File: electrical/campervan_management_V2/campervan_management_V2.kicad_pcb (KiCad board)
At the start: 4 copper layers, 140 x 95 mm, 163 parts, among them J1 Battery & Fuse, J10 RS485, J11 Power On/Off Switch, J2 Battery 2, J3 Relays, J5 Input Flow Sensor, J6 Temp, J7 Output Flow Sensor, J8 Starter Battery, J9 Fans, K1 G6KU-2, Q1 Q_PMOS_DGS, Q10 Q_PMOS_DGS, Q2 Q_PMOS_DGS, Q4 MMBT2222A, Q6 MMBT2222A, Q7 Q_PMOS_DGS, Q8 Q_PMOS_DGS, Q9 Q_PMOS_DGS, SW1 SW_Push, U1 MCP16311T-E/MNS, U10 LM358DR2G, U11 LM358DR2G, U12 LTV-817S-TA1-C, U13 LTV-817S-TA1-C, U14 HCNR200-500E, U15 LM358DR2G, U16 LTV-817S-TA1-C, U17 LTV-817S-TA1-C, U18 LTV-817S-TA1-C, U19 MAX487E, U2 AMS1117-3.3, U20 LTV-817S-TA1-C, U21 LTV-817S-TA1-C, U22 LTV-817S-TA1-C, U23 LTV-817S-TA1-C, U24 LTV-817S-TA1-C, U25 MCP16311T-E/MNS, U3 LTV-817S-TA1-C, U4 HCNR200-500E, U5 AMS1117-3.3, U6 LM358DR2G, U7 LM358DR2G, U8 LTV-817S-TA1-C, U9 HCNR200-500E

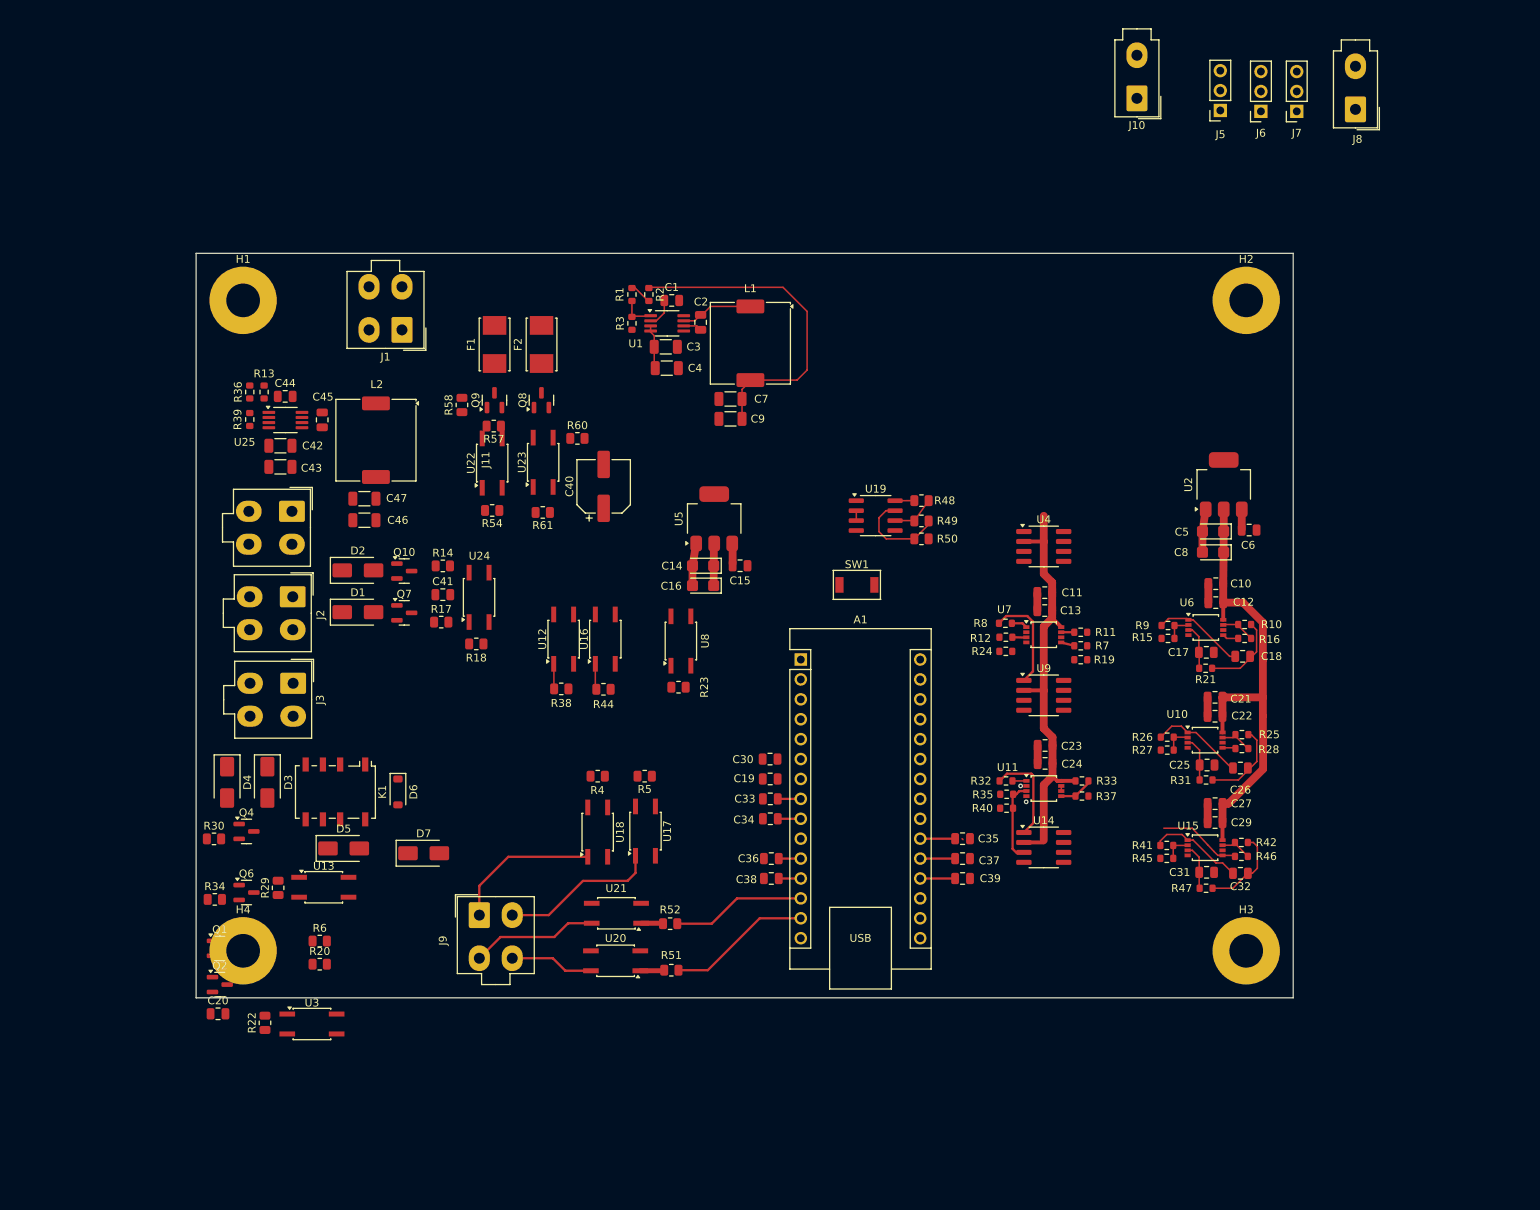
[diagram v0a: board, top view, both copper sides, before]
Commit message: First attempt at PCB layout
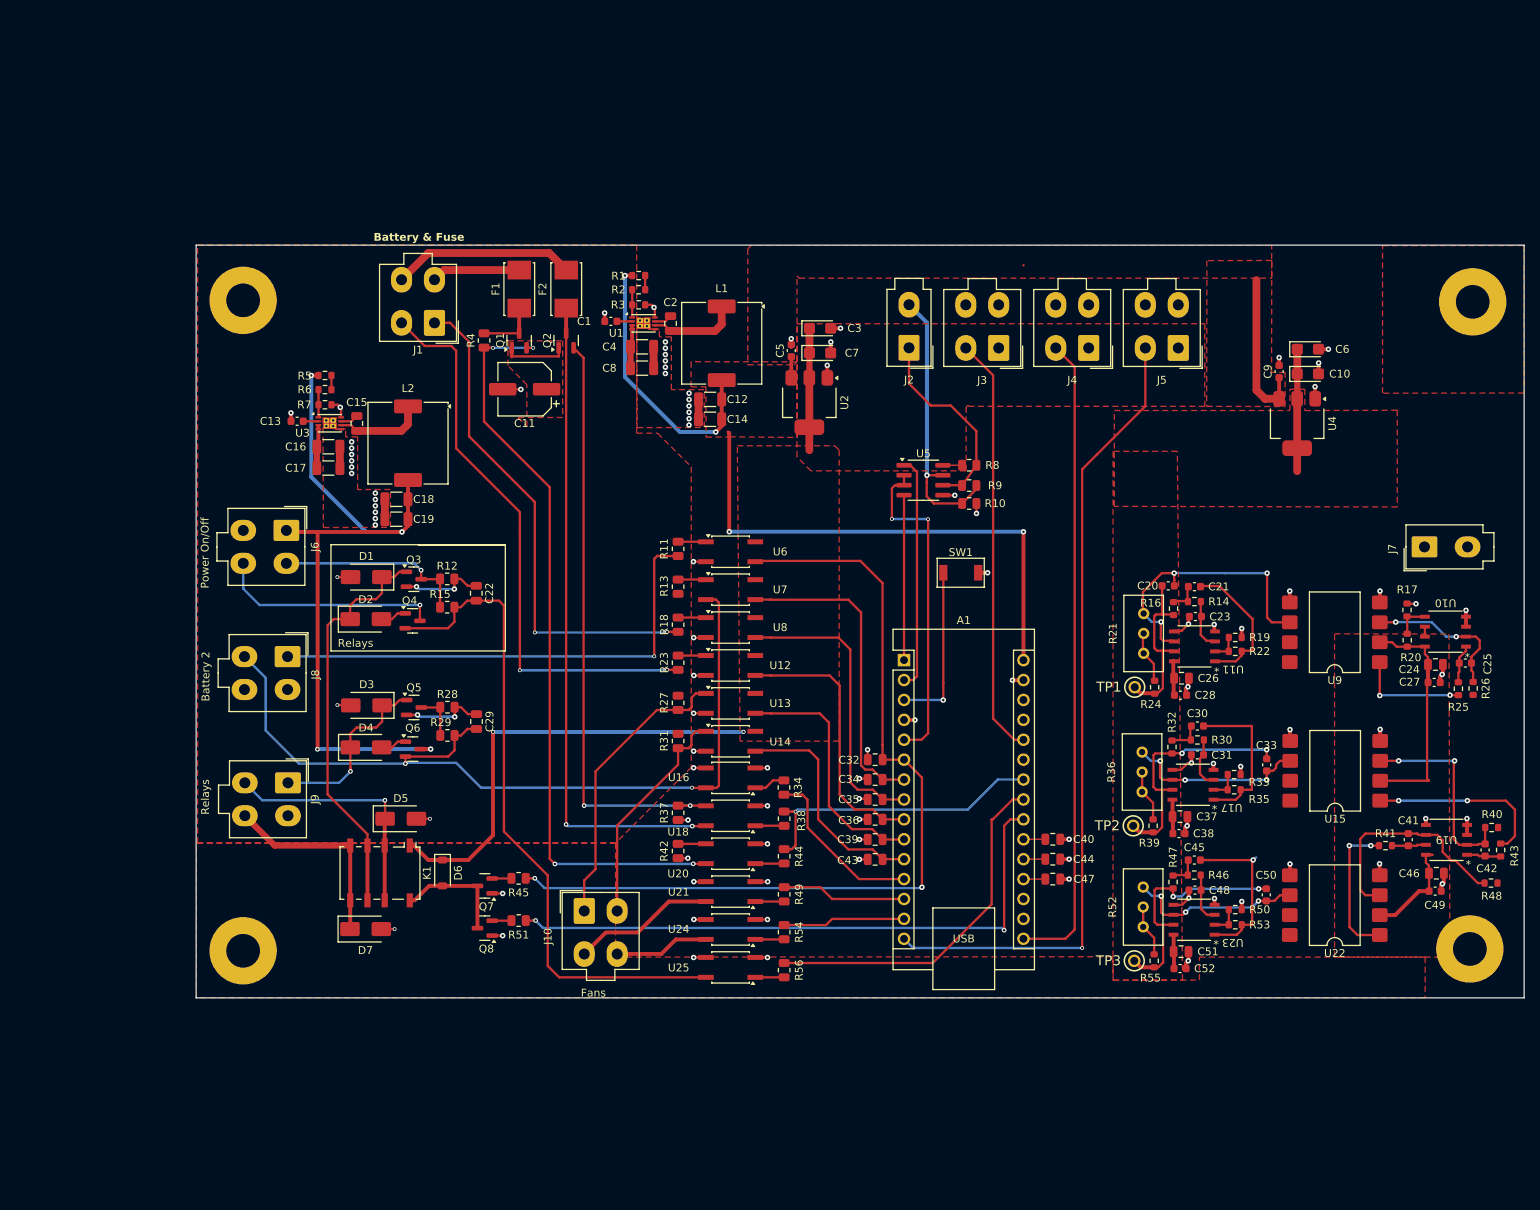
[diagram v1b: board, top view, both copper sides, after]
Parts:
- removed the C14 at (114.7, 94.9)
- removed the C15 at (119.4, 94.9)
- removed the C16 at (114.7, 97.4)
- removed the C8 at (179.8, 93.2)
- removed the J6 at (185.9, 36.9)
- removed the J7 at (190.4, 36.9)
- removed the R19 at (162.9, 106.9)
- removed the R24 at (153.3, 105.8)
- removed the R40 at (153.4, 125.8)
- removed the U5 at (116.1, 88.9)
- added C10: 10uF, Capacitor_Tantalum_SMD:CP_EIA-3216-18_Kemet-A, F.Cu at (191.9, 70.4)
- added C20: C_Small, Capacitor_SMD:C_0603_1608Metric, F.Cu at (174.0, 97.4)
- added C25: C_Small, Capacitor_SMD:C_0603_1608Metric, F.Cu at (212.0, 107.3)
- added C3: 10uF, Capacitor_Tantalum_SMD:CP_EIA-3216-18_Kemet-A, F.Cu at (129.6, 64.6)
- added C33: C_Small, Capacitor_SMD:C_0603_1608Metric, F.Cu at (186.6, 120.3)
- added C41: C_Small, Capacitor_SMD:C_0603_1608Metric, F.Cu at (204.7, 129.8)
- added C42: C_Small, Capacitor_SMD:C_0603_1608Metric, F.Cu at (214.5, 131.1)
- added C50: C_Small, Capacitor_SMD:C_0603_1608Metric, F.Cu at (186.6, 136.9)
- added C7: 10uF, Capacitor_Tantalum_SMD:CP_EIA-3216-18_Kemet-A, F.Cu at (129.6, 67.7)
- added C9: 1uF, Capacitor_SMD:C_0603_1608Metric, F.Cu at (188.2, 70.1)
- added J3: Temp, Connector_Molex:Molex_Mini-Fit_Jr_5566-04A_2x02_P4.20mm_Vertical, F.Cu at (152.4, 67.1)
- added J4: Output Flow Sensor, Connector_Molex:Molex_Mini-Fit_Jr_5566-04A_2x02_P4.20mm_Vertical, F.Cu at (163.9, 67.1)
- added R21: 10k, Potentiometer_THT:Potentiometer_Bourns_3296W_Vertical, F.Cu at (170.9, 106.0)
- added R36: 10k, Potentiometer_THT:Potentiometer_Bourns_3296W_Vertical, F.Cu at (170.7, 123.7)
- added R52: 10k, Potentiometer_THT:Potentiometer_Bourns_3296W_Vertical, F.Cu at (170.9, 141.0)
- added TP1: TestPoint, CV_connector:5000, F.Cu at (169.8, 110.4)
- added TP2: TestPoint, CV_connector:5000, F.Cu at (169.6, 128.1)
- added TP3: TestPoint, CV_connector:5000, F.Cu at (169.7, 145.3)
- added U4: AMS1117-3.3, Package_TO_SOT_SMD:SOT-223-3_TabPin2, F.Cu at (190.5, 76.7)
- C1: footprint Capacitor_SMD:C_0805_2012Metric -> Capacitor_SMD:C_0603_1608Metric
- C13: renamed from C44; footprint Capacitor_SMD:C_0805_2012Metric -> Capacitor_SMD:C_0603_1608Metric
- C21: renamed from C32; footprint Capacitor_SMD:C_0805_2012Metric -> Capacitor_SMD:C_0603_1608Metric
- C23: renamed from C31; footprint Capacitor_SMD:C_0805_2012Metric -> Capacitor_SMD:C_0603_1608Metric
- C27: renamed from C23; footprint Capacitor_SMD:C_0805_2012Metric -> Capacitor_SMD:C_0603_1608Metric
- C28: renamed from C27; footprint Capacitor_SMD:C_0805_2012Metric -> Capacitor_SMD:C_0603_1608Metric
- C30: renamed from C26; footprint Capacitor_SMD:C_0805_2012Metric -> Capacitor_SMD:C_0603_1608Metric
- C31: renamed from C25; footprint Capacitor_SMD:C_0805_2012Metric -> Capacitor_SMD:C_0603_1608Metric
- C38: renamed from C22; footprint Capacitor_SMD:C_0805_2012Metric -> Capacitor_SMD:C_0603_1608Metric
- C45: renamed from C18; footprint Capacitor_SMD:C_0805_2012Metric -> Capacitor_SMD:C_0603_1608Metric
- C48: renamed from C17; footprint Capacitor_SMD:C_0805_2012Metric -> Capacitor_SMD:C_0603_1608Metric
- C49: renamed from C11; footprint Capacitor_SMD:C_0805_2012Metric -> Capacitor_SMD:C_0603_1608Metric
- C5: value 10uF -> 1uF; footprint Capacitor_Tantalum_SMD:CP_EIA-3216-18_Kemet-A -> Capacitor_SMD:C_0603_1608Metric
- C52: renamed from C10; footprint Capacitor_SMD:C_0805_2012Metric -> Capacitor_SMD:C_0603_1608Metric
- C6: value 1uF -> 10uF; footprint Capacitor_SMD:C_0805_2012Metric -> Capacitor_Tantalum_SMD:CP_EIA-3216-18_Kemet-A
- J5: footprint Connector_PinSocket_2.54mm:PinSocket_1x03_P2.54mm_Vertical -> Connector_Molex:Molex_Mini-Fit_Jr_5566-04A_2x02_P4.20mm_Vertical
- R26: renamed from R35; value 10k -> 220k
- R40: renamed from R12; value 10k -> 220k
- R48: renamed from R7; value 10k -> 220k
- U1: value MCP16311T-E/MNS -> MCP16311x-xMNY; footprint Package_SO:MSOP-8_3x3mm_P0.65mm -> Package_DFN_QFN:DFN-8-1EP_3x2mm_P0.5mm_EP1.75x1.45mm
- U10: renamed from U11; footprint Package_SO:OnSemi_Micro8 -> CV_connector:SOIC-8_ONS-L
- U11: renamed from U15; footprint Package_SO:OnSemi_Micro8 -> CV_connector:SOIC-8_ONS-L
- U15: renamed from U9; footprint Package_SO:SOP-8_3.76x4.96mm_P1.27mm -> Package_DIP:SMDIP-8_W11.48mm
- U17: renamed from U10; footprint Package_SO:OnSemi_Micro8 -> CV_connector:SOIC-8_ONS-L
- U19: renamed from U7; footprint Package_SO:OnSemi_Micro8 -> CV_connector:SOIC-8_ONS-L
- U2: footprint CV_connector:SOT-223-3_TabPin1 -> Package_TO_SOT_SMD:SOT-223-3_TabPin2
- U22: renamed from U4; footprint Package_SO:SOP-8_3.76x4.96mm_P1.27mm -> Package_DIP:SMDIP-8_W11.48mm
- U23: renamed from U6; footprint Package_SO:OnSemi_Micro8 -> CV_connector:SOIC-8_ONS-L
- U3: renamed from U25; value MCP16311T-E/MNS -> MCP16311x-xMNY; footprint Package_SO:MSOP-8_3x3mm_P0.65mm -> Package_DFN_QFN:DFN-8-1EP_3x2mm_P0.5mm_EP1.75x1.45mm
- U9: renamed from U14; footprint Package_SO:SOP-8_3.76x4.96mm_P1.27mm -> Package_DIP:SMDIP-8_W11.48mm
- moved R43 69.5 mm to (216.5, 131.1), turned to 90 degrees
- moved U6 67.3 mm to (118.2, 93.1)
- moved R11 66.9 mm to (111.5, 92.7), turned to -90 degrees
- moved R56 66.6 mm to (125.0, 146.5), turned to -90 degrees
- moved R40 66.6 mm to (215.3, 128.3), turned to 180 degrees
- moved C22 63.0 mm to (85.8, 98.4), turned to -90 degrees
- moved C49 62.7 mm to (208.1, 136.4), turned to 0 degrees
- moved R26 61.0 mm to (213.0, 110.5), turned to 90 degrees
- moved R48 60.5 mm to (215.2, 135.4)
- moved C46 60.2 mm to (208.3, 134.1), turned to 0 degrees
- moved R42 59.1 mm to (111.5, 131.3), turned to -90 degrees
- moved U22 58.9 mm to (195.3, 138.2), turned to 180 degrees
- moved R25 58.9 mm to (211.1, 110.6), turned to -90 degrees
- moved C5 58.6 mm to (126.0, 67.4), turned to 90 degrees
- moved U20 58.4 mm to (118.2, 131.6), turned to 180 degrees
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- renumbered C40 to C11, C7 to C12, C9 to C14, C45 to C15, C42 to C16, C43 to C17, C47 to C18, C46 to C19, C20 to C22, C29 to C26, C41 to C29, C30 to C32, C19 to C34, C33 to C35, C34 to C36, C21 to C37, C36 to C39, C3 to C4, C35 to C40, C38 to C43, C37 to C44, C13 to C46, C39 to C47, C12 to C51, C4 to C8, D7 to D1, D5 to D2, D1 to D3, D2 to D4, D4 to D5, D3 to D7, J9 to J10, J10 to J2, J11 to J6, J8 to J7, J2 to J8, J3 to J9, Q9 to Q1, Q8 to Q2, Q2 to Q3, Q1 to Q4, Q7 to Q5, Q10 to Q6, Q4 to Q7, Q6 to Q8, R2 to R1, R50 to R10, R29 to R11, R6 to R12, R23 to R13, R47 to R14, R20 to R15, R42 to R16, R37 to R17, R38 to R18, R45 to R19, R1 to R2, R33 to R20, R41 to R22, R44 to R23, R46 to R24, R32 to R25, R5 to R27, R14 to R28, R17 to R29, R31 to R30, R4 to R31, R25 to R32, R27 to R33, R18 to R34, R26 to R35, R60 to R37, R61 to R38, R28 to R39, R58 to R4, R11 to R41, R57 to R42, R8 to R43, R54 to R44, R30 to R45, R21 to R46, R10 to R47, R52 to R49, R13 to R5, R15 to R50, R34 to R51, R9 to R53, R51 to R54, R16 to R55, R22 to R56, R36 to R6, R39 to R7, R48 to R8, R49 to R9, U16 to U12, U17 to U13, U18 to U14, U24 to U16, U23 to U18, U22 to U20, U20 to U24, U3 to U25, U19 to U5, U13 to U6, U8 to U7, U12 to U8
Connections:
- A1 pad 10: /Solar Charge Management/Solar Charge Battery 2 On -> /Battery Box Fan2 Sensor
- A1 pad 11: /Battery Box Fan2 Sensor -> /Battery Box Fan1 Sensor
- A1 pad 12: /Battery Box Fan1 Sensor -> /Solar Charge Management/Solar Charge Battery 2 On
- A1 pad 19: /Battery Voltage Measurement/Battery 1 Voltage -> /Battery Voltage Measurement/Starter Battery Voltage
- A1 pad 20: /Battery Voltage Measurement/Battery 2 Voltage -> /Battery Voltage Measurement/Battery 1 Voltage
- A1 pad 21: /Battery Voltage Measurement/Starter Battery Voltage -> /Battery Voltage Measurement/Battery 2 Voltage
- C15 pad 1: Net-(U25-SW) -> Net-(U25-BOOST)
- C15 pad 2: Net-(U25-BOOST) -> Net-(U25-SW)
- C2 pad 1: Net-(U1-SW) -> Net-(U1-BOOST)
- C2 pad 2: Net-(U1-BOOST) -> Net-(U1-SW)
- C40 pad 1: /Battery Voltage Measurement/Starter Battery Voltage -> /Battery Voltage Measurement/Battery 2 Voltage
- C44 pad 1: /Battery Voltage Measurement/Battery 2 Voltage -> /Battery Voltage Measurement/Battery 1 Voltage
- C47 pad 1: /Battery Voltage Measurement/Battery 1 Voltage -> /Battery Voltage Measurement/Starter Battery Voltage
- C5 pad 1: VCC_3V3A -> VCC_7V
- C6 pad 1: VCC_7V -> VCC_3V3A
- J1 pad 1: /Battery Voltage Measurement/Battery 1 Vin -> /Battery Fuse Sensors/Battery 1 Fuse Sensor
- J1 pad 2: /Battery Voltage Measurement/Battery 2 Vin -> /Battery Fuse Sensors/Battery 2 Fuse Sensor
- J1 pad 3: /Battery Fuse Sensors/Battery 1 Fuse Sensor -> /Battery Voltage Measurement/Battery 2 Vin
- J1 pad 4: /Battery Fuse Sensors/Battery 2 Fuse Sensor -> /Battery Voltage Measurement/Battery 1 Vin
- L1 pad 1: Net-(U1-BOOST) -> Net-(U1-SW)
- L2 pad 1: Net-(U25-BOOST) -> Net-(U25-SW)
- R24 pad 1: Net-(U15B-+) -> Net-(R40-Pad1)
- R26 pad 2: Net-(U11A-+) -> Net-(U11A--)
- R27 pad 2: Net-(J9-Pin_2) -> Net-(J9-Pin_1)
- R31 pad 2: Net-(J9-Pin_1) -> Net-(J9-Pin_2)
- R39 pad 1: Net-(U10B-+) -> Net-(R19-Pad1)
- R40 pad 2: Net-(U7A-+) -> Net-(U7A--)
- R48 pad 2: Net-(U7B-+) -> Net-(U7B--)
- R55 pad 1: Net-(U6B-+) -> Net-(R16-Pad1)
- U10 pad 2: GND -> Net-(U11A--)
- U10 pad 3: Net-(U11A-+) -> GND
- U11 pad 5: Net-(U15B-+) -> GND
- U11 pad 6: GND -> Net-(U15B--)
- U13 pad 1: Net-(J9-Pin_2) -> Net-(J9-Pin_1)
- U14 pad 1: Net-(J9-Pin_1) -> Net-(J9-Pin_2)
- U15 pad 3: Net-(U7A-+) -> Net-(U7A--)
- U15 pad 6: Net-(U10B-+) -> Net-(U10B--)
- U17 pad 5: Net-(U10B-+) -> GND
- U17 pad 6: GND -> Net-(U10B--)
- U19 pad 2: GND -> Net-(U7A--)
- U19 pad 3: Net-(U7A-+) -> GND
- U19 pad 5: Net-(U7B-+) -> GND
- U19 pad 6: GND -> Net-(U7B--)
- U2 pad 2: VCC_3V3A -> VCC_3V3
- U22 pad 3: Net-(U7B-+) -> Net-(U7B--)
- U22 pad 6: Net-(U6B-+) -> Net-(U6B--)
- U23 pad 5: Net-(U6B-+) -> GND
- U23 pad 6: GND -> Net-(U6B--)
- U9 pad 3: Net-(U11A-+) -> Net-(U11A--)
- U9 pad 6: Net-(U15B-+) -> Net-(U15B--)
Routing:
- net /Battery 2 On/Off Switch Sensor: track 0.00 -> 111.1 mm, vias 0 -> 2
- net /Solar Charge Management/Solar Charge Battery 2 Switch: track 0.00 -> 109.3 mm, vias 0 -> 2
- net GND: track 23.4 -> 130.3 mm, vias 0 -> 98
- net /Input Flow Sensor: track 0.00 -> 103.4 mm, vias 0 -> 1
- net Net-(Q9-G): track 0.00 -> 96.1 mm, vias 0 -> 4
- net VCC_4V1: track 0.00 -> 93.7 mm, vias 0 -> 4
- net Net-(Q1-G): track 0.00 -> 84.5 mm
- net Net-(Q8-S): track 0.00 -> 83.8 mm, vias 0 -> 2
- net /Output Flow Sensor: track 0.00 -> 82.3 mm
- net /Battery 2 On/Off: track 0.00 -> 77.7 mm, vias 0 -> 2
- net VCC_7V: track 47.5 -> 125.0 mm, vias 0 -> 4
- net Net-(Q8-G): track 0.00 -> 76.1 mm, vias 0 -> 2
- net /Battery Fuse Sensors/Battery 2 Fuse Sensor: track 0.00 -> 72.8 mm, vias 0 -> 2
- net VCC_3V3: track 7.68 -> 75.9 mm, vias 0 -> 2
- net /Battery Fuse Sensors/Battery 1 Fuse Sensor: track 0.00 -> 64.3 mm, vias 0 -> 2
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- added copper zone on F.Cu, net GND
- added copper zone on In1.Cu, net GND
- added copper zone on In2.Cu, net GND
- added copper zone on F.Cu, net VCC_3V3
- added copper zone on F.Cu, net VCC_3V3A
- added copper zone on F.Cu, net VCC_7V
- added copper zone on F.Cu, net VIN
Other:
- board size 140 x 95 mm -> 169.5 x 96 mm
- board text added: "Battery & Fuse"
- board text added: "Battery 2"
- board text added: "Fans"
- board text added: "Power On/Off"
- board text added: "Relays"
- board text removed: "Battery Management"
- board text removed: "Fan management"
- board text removed: "Solar Charge Switch"

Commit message: Close to final design
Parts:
- removed the J8 at (61.7, 106.5)
- removed the R42 at (111.5, 131.3)
- added C14: 220pF, Capacitor_SMD:C_0805_2012Metric, F.Cu at (90.8, 60.0)
- added D1: 1N418W, Diode_SMD:D_SOD-123, F.Cu at (96.5, 48.5)
- added D2: 1N418W, Diode_SMD:D_SOD-123, F.Cu at (101.7, 48.5)
- added D4: 1N418W, Diode_SMD:D_SOD-123, F.Cu at (91.5, 64.2)
- added J2: Battery 2, Connector_Molex:Molex_Mini-Fit_Jr_5566-02A_2x01_P4.20mm_Vertical, F.Cu at (43.3, 47.4)
- added J3: Solar Charge, Connector_Molex:Molex_Mini-Fit_Jr_5566-02A_2x01_P4.20mm_Vertical, F.Cu at (43.3, 54.8)
- added R9: 330, Resistor_SMD:R_0805_2012Metric, F.Cu at (90.8, 56.3)
- C11: footprint Capacitor_SMD:CP_Elec_6.3x5.9 -> Capacitor_THT:C_Radial_D6.3mm_H11.0mm_P2.50mm
- F1: renamed from F2; footprint Fuse:Fuseholder_Littelfuse_Nano2_157x -> Fuse:Fuse_1812_4532Metric
- F2: renamed from F1; footprint Fuse:Fuseholder_Littelfuse_Nano2_157x -> Fuse:Fuse_1812_4532Metric
- K1: value G6KU-2 -> G5V-2; footprint Relay_SMD:Relay_DPDT_Omron_G6K-2F-Y -> Relay_THT:Relay_DPDT_Omron_G5V-2
- Q1, Q2, Q3, Q4, Q5, Q6: value Q_PMOS_DGS -> FDS4685; footprint Package_TO_SOT_SMD:SOT-23 -> Package_SO:SOIC-8_3.9x4.9mm_P1.27mm
- R51: renamed from R24; value 22k -> 10k
- R52: renamed from R39; value 22k -> 10k
- R53: renamed from R55; value 22k -> 10k
- R7: renamed from R4; value 47k -> 1k
- R8: renamed from R37; value 47k -> 27k
- U22: renamed from U4; value AMS1117-3.3 -> AMS1117-3.3/TLV761
- U5: renamed from U2; value AMS1117-3.3 -> AMS1117-3.3/TLV761
- moved J9 166.2 mm to (43.0, 120.5), turned to -90 degrees
- moved U17 162.8 mm to (48.5, 127.8), turned to -90 degrees
- moved R36 162.0 mm to (45.7, 132.7), turned to 180 degrees
- moved C30 160.5 mm to (52.5, 125.3), turned to 90 degrees
- moved R34 157.8 mm to (55.7, 124.3), turned to 180 degrees
- moved R37 157.5 mm to (49.6, 132.7), turned to 180 degrees
- moved C31 157.0 mm to (52.7, 129.1), turned to 90 degrees
- moved R35 156.1 mm to (55.7, 126.2), turned to 0 degrees
- moved C34 154.3 mm to (55.0, 129.3), turned to 90 degrees
- moved U20 151.7 mm to (48.5, 141.9), turned to -90 degrees
- moved C43 148.4 mm to (42.7, 159.8), turned to 90 degrees
- moved C53 147.0 mm to (42.6, 163.2), turned to 90 degrees
- moved R46 145.9 mm to (44.6, 159.8), turned to 90 degrees
- moved C44 143.4 mm to (46.5, 159.7), turned to -90 degrees
- moved R48 143.4 mm to (45.5, 162.5), turned to 180 degrees
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- renumbered C13 to C1, C18 to C10, C14 to C13, C5 to C15, C29 to C16, C3 to C17, C7 to C18, C22 to C19, C15 to C2, C32 to C20, C34 to C21, C35 to C22, C43 to C23, C36 to C24, C39 to C25, C40 to C26, C44 to C27, C47 to C28, C42 to C29, C1 to C3, C25 to C30, C24 to C31, C46 to C32, C49 to C33, C27 to C34, C41 to C35, C9 to C36, C6 to C37, C10 to C38, C33 to C39, C2 to C4, C50 to C40, C30 to C41, C31 to C42, C21 to C43, C23 to C44, C48 to C46, C26 to C47, C51 to C48, C28 to C49, C16 to C5, C37 to C50, C38 to C51, C20 to C53, C17 to C6, C4 to C7, C19 to C9, D7 to D10, D4 to D5, D1 to D6, D2 to D7, D5 to D8, D6 to D9, H4 to H3, H3 to H4, J4 to J10, J5 to J11, J6 to J4, J2 to J5, J10 to J6, J9 to J7, J3 to J8, J7 to J9, L2 to L1, L1 to L2, R5 to R1, R28 to R10, R44 to R11, R38 to R12, R29 to R13, R11 to R14, R13 to R15, R8 to R16, R9 to R17, R10 to R18, R18 to R19, R6 to R2, R54 to R20, R23 to R21, R12 to R22, R49 to R23, R15 to R24, R34 to R25, R56 to R26, R31 to R27, R27 to R28, R45 to R29, R1 to R3, R51 to R30, R43 to R31, R40 to R32, R48 to R33, R26 to R34, R25 to R35, R17 to R36, R20 to R37, R41 to R38, R19 to R39, R7 to R4, R22 to R40, R33 to R41, R35 to R42, R50 to R43, R53 to R44, R30 to R45, R14 to R46, R46 to R47, R16 to R48, R32 to R49, R2 to R5, R47 to R50, R21 to R54, R36 to R55, R52 to R56, R3 to R6, U3 to U1, U12 to U10, U24 to U11, U16 to U12, U21 to U13, U25 to U15, U13 to U16, U10 to U17, U19 to U18, U15 to U19, U1 to U2, U9 to U20, U22 to U21, U11 to U23, U17 to U24, U23 to U25, U20 to U3, U18 to U4, U5 to U8, U8 to U9
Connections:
- A1 pad 10: /Battery Box Fan2 Sensor -> unconnected-(A1-D7-Pad10)
- A1 pad 11: /Battery Box Fan1 Sensor -> /Solar Charge Management/Solar Charge Battery 2 On
- A1 pad 12: /Solar Charge Management/Solar Charge Battery 2 On -> /Batteries On
- A1 pad 13: /Battery Box Fan1 Control -> /Battery 2 On/Off
- A1 pad 14: /Battery Box Fan2 Control -> /Power Supply Control
- A1 pad 19: /Battery Voltage Measurement/Starter Battery Voltage -> /Battery Voltage Measurement/Battery 2 Voltage
- A1 pad 21: /Battery Voltage Measurement/Battery 2 Voltage -> /Battery Voltage Measurement/Starter Battery Voltage
- A1 pad 22: /Battery 2 On/Off -> /Battery Box Fan2 Sensor
- A1 pad 23: /Batteries On -> /Battery Box Fan1 Sensor
- A1 pad 24: /Power Supply Control -> /Battery Box Fan1 Control
- A1 pad 25: unconnected-(A1-A6-Pad25) -> /Battery Box Fan2 Control
- C16 pad 1: Net-(Q7-G) -> Net-(Q3-G)
- C19 pad 1: Net-(Q2-G) -> Net-(Q5-G)
- C19 pad 2: Net-(Q1-G) -> Net-(Q6-G)
- C26 pad 1: /Battery Voltage Measurement/Battery 2 Voltage -> /Battery Voltage Measurement/Starter Battery Voltage
- C28 pad 1: /Battery Voltage Measurement/Starter Battery Voltage -> /Battery Voltage Measurement/Battery 2 Voltage
- D5 pad 2: Net-(D2-A) -> /Solar Charge Management/test
- D6 pad 1: Net-(D5-K) -> Net-(D6-K)
- D7 pad 1: Net-(D5-K) -> Net-(D6-K)
- D7 pad 2: Net-(D5-A) -> Net-(D7-A)
- D9 pad 2: Net-(D6-A) -> Net-(D9-A)
- F1 pad 1: Net-(Q8-S) -> Net-(D2-A)
- F1 pad 2: /Battery Voltage Measurement/Battery 1 Vin -> /Battery Voltage Measurement/Battery 2 Vin
- F2 pad 1: Net-(Q9-S) -> Net-(D1-A)
- F2 pad 2: /Battery Voltage Measurement/Battery 2 Vin -> /Battery Voltage Measurement/Battery 1 Vin
- J1 pad 1: /Battery Fuse Sensors/Battery 1 Fuse Sensor -> /Battery Voltage Measurement/Battery 1 Vin
- J1 pad 4: /Battery Voltage Measurement/Battery 1 Vin -> /Battery Fuse Sensors/Battery 1 Fuse Sensor
- K1 pad 4: /Battery Management/Battery 1 Relay -> Net-(D6-K)
- K1 pad 6: Net-(D5-K) -> /Battery Management/Battery 2 Relay
- K1 pad 8: Net-(D6-A) -> /Battery Management/Battery 1 Relay
- Q1 pad 1: VIN -> Net-(D2-A)
- Q1 pad 2: Net-(Q9-G) -> Net-(D2-A)
- Q1 pad 3: Net-(Q9-S) -> Net-(D2-A)
- Q2 pad 1: VIN -> Net-(D1-A)
- Q2 pad 2: Net-(Q8-G) -> Net-(D1-A)
- Q2 pad 3: Net-(Q8-S) -> Net-(D1-A)
- Q3 pad 1: Net-(D5-K) -> VIN
- Q3 pad 2: Net-(Q2-G) -> VIN
- Q3 pad 3: /Battery Management/Power On Switch - 4V1 -> VIN
- Q4 pad 1: Net-(D5-A) -> VCC_4V1
- Q4 pad 2: Net-(Q1-G) -> VCC_4V1
- Q4 pad 3: /Battery Management/Power On Switch - Vin -> VCC_4V1
- Q5 pad 1: /Solar Charge Battery 2 Relay -> /Battery Management/Power On Switch - 4V1
- Q5 pad 2: Net-(Q7-G) -> /Battery Management/Power On Switch - 4V1
- Q5 pad 3: VIN -> /Battery Management/Power On Switch - 4V1
- Q6 pad 1: Net-(D2-A) -> /Battery Management/Power On Switch - Vin
- Q6 pad 2: /Solar Charge Management/Solar Charge Battery 2 Switch -> /Battery Management/Power On Switch - Vin
- Q6 pad 3: VCC_4V1 -> /Battery Management/Power On Switch - Vin
- Q7 pad 3: Net-(D6-A) -> Net-(D9-A)
- Q8 pad 3: Net-(D6-A) -> Net-(D9-A)
- R10 pad 2: Net-(Q7-G) -> Net-(Q3-G)
- R22 pad 2: Net-(Q2-G) -> Net-(Q5-G)
- R24 pad 2: Net-(Q1-G) -> Net-(Q6-G)
- R7 pad 1: Net-(Q9-S) -> /Power Supply/Vps
- R7 pad 2: Net-(Q9-G) -> Net-(Q2-G)
- R8 pad 1: Net-(Q8-G) -> Net-(Q1-G)
- U15 pad 4: Net-(Q1-G) -> Net-(Q6-G)
- U3 pad 3: Net-(R57-Pad1) -> GND
- U3 pad 4: Net-(Q9-G) -> Net-(Q2-G)
- U4 pad 3: Net-(Q8-G) -> Net-(Q1-G)
- U4 pad 4: Net-(Q8-S) -> /Power Supply/Vps
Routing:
- net VIN: track 69.6 -> 166.9 mm, vias 0 -> 4
- net /Battery Voltage Measurement/Starter Battery Voltage: track 21.1 -> 117.7 mm, vias 0 -> 1
- net Net-(Q9-G): track 96.1 -> 0.00 mm, vias 4 -> 0
- net /Battery Voltage Measurement/Battery 2 Vin: track 11.3 -> 100.2 mm
- net Net-(Q8-S): track 83.8 -> 0.00 mm, vias 2 -> 0
- net /Battery Voltage Measurement/Battery 1 Vin: track 23.3 -> 101.7 mm, vias 0 -> 4
- net /Battery Voltage Measurement/Battery 1 Voltage: track 23.0 -> 99.3 mm, vias 0 -> 1
- net Net-(Q8-G): track 76.1 -> 0.00 mm, vias 2 -> 0
- net /Battery 2 On/Off: track 77.7 -> 12.0 mm, vias 2 -> 1
- net /Battery Voltage Measurement/Battery 2 Voltage: track 24.2 -> 84.8 mm
- net VCC_4V1: track 93.7 -> 35.3 mm, vias 4 -> 2
- net Net-(Q1-G): track 84.5 -> 27.5 mm
- net /Solar Charge Battery 2 Relay: track 23.6 -> 78.4 mm, vias 1 -> 8
- net VCC_3V3: track 75.9 -> 22.5 mm, vias 2 -> 12
- net Net-(D5-K): track 52.3 -> 0.00 mm
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- added copper zone on F.Cu, net /Battery Management/Power On Switch - 4V1
- added copper zone on F.Cu, net /Solar Charge Battery 2 Relay
- added copper zone on F.Cu, net /Solar Charge Management/test
- added copper zone on F.Cu, net Net-(D1-A)
- added copper zone on F.Cu, net Net-(D2-A)
- added copper zone on F.Cu, net Net-(D6-K)
- added copper zone on F.Cu, net Net-(D7-A)
- added copper zone on B.Cu, net VCC_3V3
- added copper zone on F.Cu, net VCC_4V1
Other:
- board size 169.5 x 96 mm -> 130 x 150 mm
- board text added: "3V3 Analogue LDO"
- board text added: "4V1"
- board text added: "7V"
- board text added: "Battery 1"
- board text added: "KladderVan V1.0"
- board text added: "Starter Batt."
- board text removed: "Battery & Fuse"
- board text removed: "Fans"
- board text removed: "Power On/Off"
